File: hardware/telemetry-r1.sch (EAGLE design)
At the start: 111 parts, among them IC1 COPERNICUSSMD, IC10 TPS70933, IC2 TPS70933, IC3 74HC137, IC4 STM32L073CZT6, IC5 TPS62160, IC6 HX1, IC7 LMP7702, IC8 ADXL345, IC9 HIH9131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

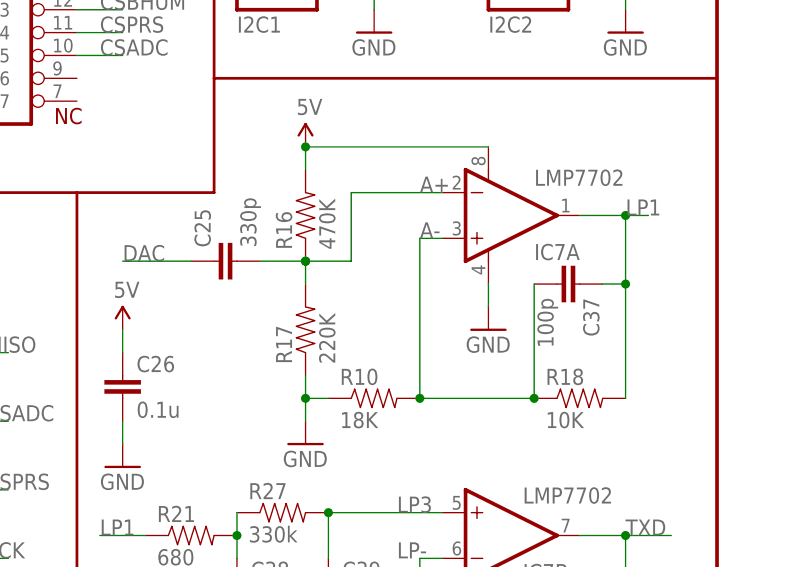
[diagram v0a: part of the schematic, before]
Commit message: Fixed swapped pins in DAC filter
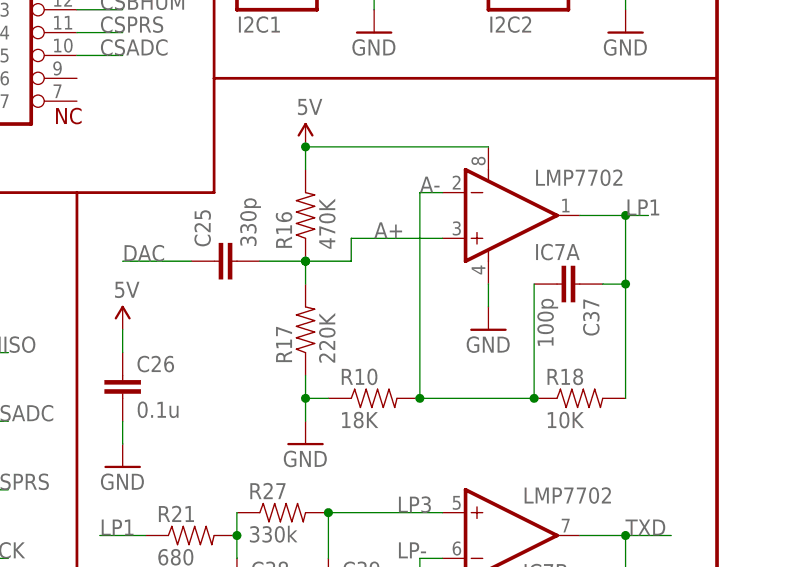
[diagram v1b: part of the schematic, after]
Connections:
- net A+: now also IC7A.+IN; no longer IC7A.-IN
- net A-: now also IC7A.-IN; no longer IC7A.+IN
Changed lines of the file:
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@@
 <net name="A-" class="0">
 <segment>
-<wire x1="215.9" y1="139.7" x2="215.9" y2="121.92" width="0.1524" layer="91"/>
-<label x="215.9" y="139.7" size="1.778" layer="95"/>
-<pinref part="IC7" gate="A" pin="+IN"/>
-<wire x1="218.44" y1="139.7" x2="215.9" y2="139.7" width="0.1524" layer="91"/>
+<wire x1="215.9" y1="144.78" x2="215.9" y2="121.92" width="0.1524" layer="91"/>
 <pinref part="R10" gate="G$1" pin="2"/>
 <pinref part="C37" gate="G$1" pin="2"/>
@@
 <junction x="228.6" y="121.92"/>
 <junction x="215.9" y="121.92"/>
+<pinref part="IC7" gate="A" pin="-IN"/>
+<wire x1="215.9" y1="144.78" x2="218.44" y2="144.78" width="0.1524" layer="91"/>
+<label x="215.9" y="144.78" size="1.778" layer="95"/>
 </segment>
 </net>
@@
 <junction x="203.2" y="137.16"/>
 <junction x="203.2" y="137.16"/>
-<label x="215.9" y="144.78" size="1.778" layer="95"/>
-<wire x1="208.28" y1="144.78" x2="208.28" y2="137.16" width="0.1524" layer="91"/>
+<wire x1="208.28" y1="139.7" x2="208.28" y2="137.16" width="0.1524" layer="91"/>
 <wire x1="208.28" y1="137.16" x2="203.2" y2="137.16" width="0.1524" layer="91"/>
-<pinref part="IC7" gate="A" pin="-IN"/>
-<wire x1="218.44" y1="144.78" x2="208.28" y2="144.78" width="0.1524" layer="91"/>
+<pinref part="IC7" gate="A" pin="+IN"/>
+<wire x1="218.44" y1="139.7" x2="208.28" y2="139.7" width="0.1524" layer="91"/>
+<label x="210.82" y="139.7" size="1.778" layer="95"/>
 </segment>
 </net>

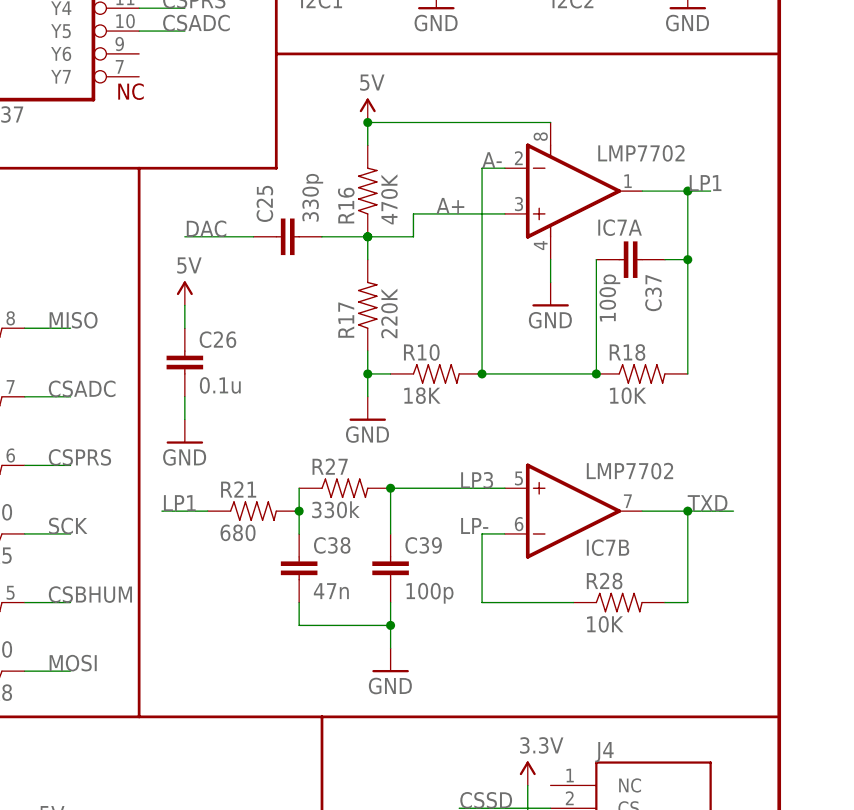
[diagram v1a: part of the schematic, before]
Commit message: Update HX1 filter to match latest experimental results
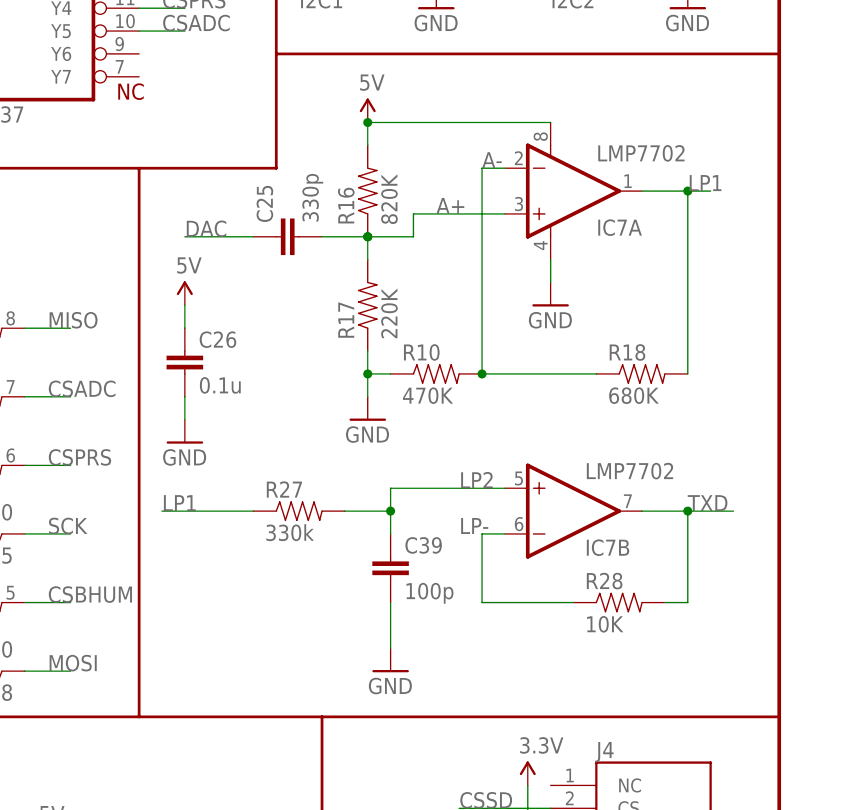
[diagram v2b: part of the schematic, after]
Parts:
- removed C37: 100p, SparkFun-Passives:CAP0805
- removed C38: 47n, SparkFun-Passives:CAP0805
- removed R21: 680, SparkFun-Passives:RESISTOR0805-RES
- R10: value 18K -> 470K
- R16: value 470K -> 820K
- R18: value 10K -> 680K
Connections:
- removed net LP3: C39.1, IC7B.+IN, R27.2
- net A-: no longer C37.2
- net GND: no longer C38.2
- net LP1: now also R27.1; no longer C37.1, R21.1
- net LP2: now also C39.1, IC7B.+IN, R27.2; no longer C38.1, R21.2, R27.1
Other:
- moved on the sheet: R27
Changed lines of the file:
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@@
 <?xml version="1.0" encoding="utf-8"?>
 <!DOCTYPE eagle SYSTEM "eagle.dtd">
-<eagle version="7.5.0">
+<eagle version="7.6.0">
 <drawing>
 <settings>
@@
 <part name="GND25" library="SparkFun-Aesthetics" deviceset="GND" device=""/>
 <part name="C25" library="SparkFun-Passives" deviceset="CAP" device="0805" value="330p"/>
-<part name="R16" library="SparkFun-Passives" deviceset="RESISTOR" device="0805-RES" value="470K"/>
+<part name="R16" library="SparkFun-Passives" deviceset="RESISTOR" device="0805-RES" value="820K"/>
 <part name="R17" library="SparkFun-Passives" deviceset="RESISTOR" device="0805-RES" value="220K"/>
-<part name="R18" library="SparkFun-Passives" deviceset="RESISTOR" device="0805-RES" value="10K"/>
+<part name="R18" library="SparkFun-Passives" deviceset="RESISTOR" device="0805-RES" value="680K"/>
 <part name="C26" library="SparkFun-Passives" deviceset="CAP" device="0805" value="0.1u"/>
 <part name="GND26" library="SparkFun-Aesthetics" deviceset="GND" device=""/>
@@
 <part name="GND48" library="SparkFun-Aesthetics" deviceset="GND" device=""/>
 <part name="SUPPLY20" library="SparkFun-Aesthetics" deviceset="3.3V" device=""/>
-<part name="C37" library="SparkFun-Passives" deviceset="CAP" device="0805" value="100p"/>
-<part name="R10" library="SparkFun-Passives" deviceset="RESISTOR" device="0805-RES" value="18K"/>
-<part name="R21" library="SparkFun-Passives" deviceset="RESISTOR" device="0805-RES" value="680"/>
-<part name="C38" library="SparkFun-Passives" deviceset="CAP" device="0805" value="47n"/>
+<part name="R10" library="SparkFun-Passives" deviceset="RESISTOR" device="0805-RES" value="470K"/>
 <part name="SUPPLY25" library="SparkFun-Aesthetics" deviceset="5V" device=""/>
 <part name="R27" library="SparkFun-Passives" deviceset="RESISTOR" device="0805-RES" value="330k"/>
@@
 <instance part="GND48" gate="1" x="279.4" y="20.32"/>
 <instance part="SUPPLY20" gate="G$1" x="279.4" y="33.02"/>
-<instance part="C37" gate="G$1" x="231.14" y="134.62" rot="R270"/>
 <instance part="R10" gate="G$1" x="210.82" y="121.92"/>
-<instance part="R21" gate="G$1" x="190.5" y="106.68"/>
-<instance part="C38" gate="G$1" x="195.58" y="99.06"/>
 <instance part="SUPPLY25" gate="G$1" x="182.88" y="129.54"/>
-<instance part="R27" gate="G$1" x="200.66" y="109.22"/>
+<instance part="R27" gate="G$1" x="195.58" y="106.68"/>
 <instance part="C39" gate="G$1" x="205.74" y="99.06"/>
 <instance part="R28" gate="G$1" x="231.14" y="96.52"/>
@@
 <segment>
 <pinref part="GND27" gate="1" pin="GND"/>
-<pinref part="C38" gate="G$1" pin="2"/>
-<wire x1="195.58" y1="96.52" x2="195.58" y2="93.98" width="0.1524" layer="91"/>
-<wire x1="195.58" y1="93.98" x2="205.74" y2="93.98" width="0.1524" layer="91"/>
 <pinref part="C39" gate="G$1" pin="2"/>
-<wire x1="205.74" y1="93.98" x2="205.74" y2="91.44" width="0.1524" layer="91"/>
-<wire x1="205.74" y1="96.52" x2="205.74" y2="93.98" width="0.1524" layer="91"/>
-<junction x="205.74" y="93.98"/>
+<wire x1="205.74" y1="96.52" x2="205.74" y2="91.44" width="0.1524" layer="91"/>
 </segment>
 <segment>
@@
 <wire x1="215.9" y1="144.78" x2="215.9" y2="121.92" width="0.1524" layer="91"/>
 <pinref part="R10" gate="G$1" pin="2"/>
-<pinref part="C37" gate="G$1" pin="2"/>
 <pinref part="R18" gate="G$1" pin="1"/>
-<wire x1="228.6" y1="134.62" x2="228.6" y2="121.92" width="0.1524" layer="91"/>
 <wire x1="228.6" y1="121.92" x2="215.9" y2="121.92" width="0.1524" layer="91"/>
-<junction x="228.6" y="121.92"/>
 <junction x="215.9" y="121.92"/>
 <pinref part="IC7" gate="A" pin="-IN"/>
@@
 <net name="LP1" class="0">
 <segment>
-<wire x1="238.76" y1="121.92" x2="238.76" y2="134.62" width="0.1524" layer="91"/>
-<wire x1="238.76" y1="134.62" x2="238.76" y2="142.24" width="0.1524" layer="91"/>
+<wire x1="238.76" y1="121.92" x2="238.76" y2="142.24" width="0.1524" layer="91"/>
 <wire x1="241.3" y1="142.24" x2="238.76" y2="142.24" width="0.1524" layer="91"/>
 <label x="238.76" y="142.24" size="1.778" layer="95"/>
@@
 <junction x="238.76" y="142.24"/>
 <pinref part="R18" gate="G$1" pin="2"/>
-<pinref part="C37" gate="G$1" pin="1"/>
-<wire x1="236.22" y1="134.62" x2="238.76" y2="134.62" width="0.1524" layer="91"/>
-<junction x="238.76" y="134.62"/>
-</segment>
-<segment>
-<pinref part="R21" gate="G$1" pin="1"/>
-<wire x1="180.34" y1="106.68" x2="185.42" y2="106.68" width="0.1524" layer="91"/>
+</segment>
+<segment>
+<pinref part="R27" gate="G$1" pin="1"/>
+<wire x1="190.5" y1="106.68" x2="180.34" y2="106.68" width="0.1524" layer="91"/>
 <label x="180.34" y="106.68" size="1.778" layer="95"/>
 </segment>
@@
 <net name="LP2" class="0">
 <segment>
-<pinref part="C38" gate="G$1" pin="1"/>
-<pinref part="R21" gate="G$1" pin="2"/>
-<wire x1="195.58" y1="104.14" x2="195.58" y2="106.68" width="0.1524" layer="91"/>
-<pinref part="R27" gate="G$1" pin="1"/>
-<wire x1="195.58" y1="109.22" x2="195.58" y2="106.68" width="0.1524" layer="91"/>
-<junction x="195.58" y="106.68"/>
-</segment>
-</net>
-<net name="LP3" class="0">
-<segment>
-<pinref part="R27" gate="G$1" pin="2"/>
 <label x="213.36" y="109.22" size="1.778" layer="95"/>
-<pinref part="C39" gate="G$1" pin="1"/>
-<wire x1="205.74" y1="104.14" x2="205.74" y2="109.22" width="0.1524" layer="91"/>
 <pinref part="IC7" gate="B" pin="+IN"/>
 <wire x1="218.44" y1="109.22" x2="205.74" y2="109.22" width="0.1524" layer="91"/>
-<junction x="205.74" y="109.22"/>
-</segment>
-</net>
+<pinref part="R27" gate="G$1" pin="2"/>
+<wire x1="200.66" y1="106.68" x2="205.74" y2="106.68" width="0.1524" layer="91"/>
+<wire x1="205.74" y1="106.68" x2="205.74" y2="109.22" width="0.1524" layer="91"/>
+<pinref part="C39" gate="G$1" pin="1"/>
+<wire x1="205.74" y1="106.68" x2="205.74" y2="104.14" width="0.1524" layer="91"/>
+<junction x="205.74" y="106.68"/>
+</segment>
+</net>

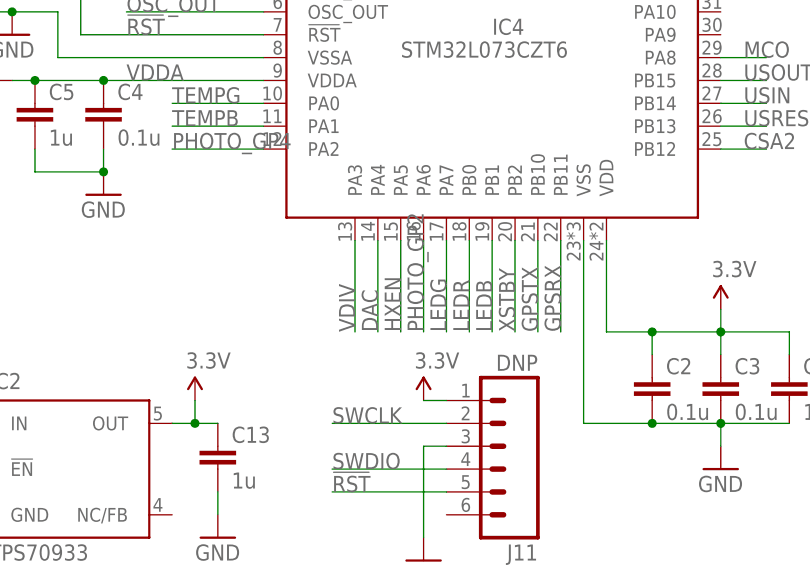
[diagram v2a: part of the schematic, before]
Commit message: Swap HXEN pin to 5VT pin
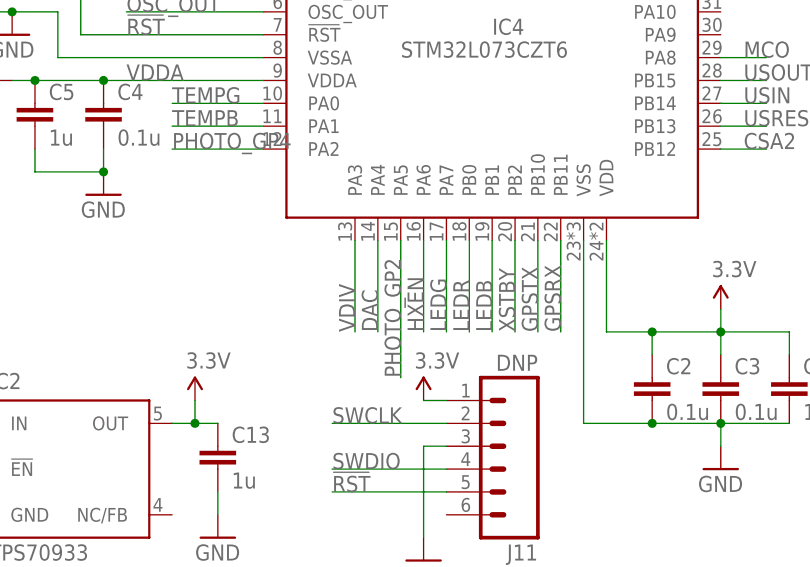
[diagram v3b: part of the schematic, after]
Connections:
- net HXEN: now also IC4.PA6; no longer IC4.PA5
- net PHOTO_GP2: now also IC4.PA5; no longer IC4.PA6
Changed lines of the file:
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@@
 </segment>
 <segment>
-<pinref part="IC4" gate="G$1" pin="PA5"/>
-<wire x1="60.96" y1="30.48" x2="60.96" y2="40.64" width="0.1524" layer="91"/>
-<label x="60.96" y="30.48" size="1.778" layer="95" rot="R90"/>
+<pinref part="IC4" gate="G$1" pin="PA6"/>
+<wire x1="63.5" y1="30.48" x2="63.5" y2="40.64" width="0.1524" layer="91"/>
+<label x="63.5" y="30.48" size="1.778" layer="95" rot="R90"/>
 </segment>
 </net>
@@
 </segment>
 <segment>
-<pinref part="IC4" gate="G$1" pin="PA6"/>
-<wire x1="63.5" y1="30.48" x2="63.5" y2="40.64" width="0.1524" layer="91"/>
-<label x="63.5" y="30.48" size="1.778" layer="95" rot="R90"/>
-</segment>
-</net>
+<pinref part="IC4" gate="G$1" pin="PA5"/>
+<wire x1="60.96" y1="25.4" x2="60.96" y2="40.64" width="0.1524" layer="91"/>
+<label x="60.96" y="25.4" size="1.778" layer="95" rot="R90"/>
+</segment>
+</net>
